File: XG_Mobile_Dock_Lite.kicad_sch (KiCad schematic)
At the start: 21 parts, among them J1 5-1775443-8, J13 39300240, J14 469911008, J17 8730, J2 20455-040E-76, J3 20455-040E-76, J4 3-2362375-4, J5 USB_C_Receptacle, SW1 SW_Push, U1 AMS1117-3.3

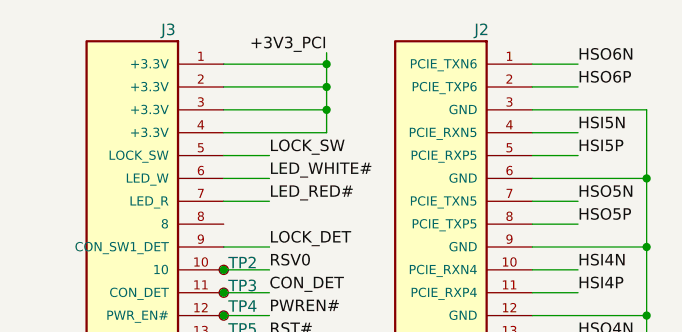
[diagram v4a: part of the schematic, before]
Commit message: pcb: fix +3.3V rail for cable LED
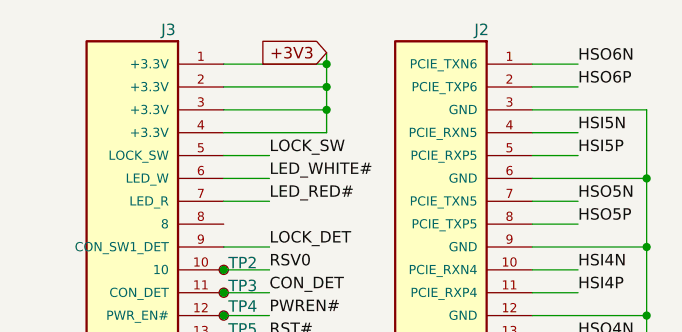
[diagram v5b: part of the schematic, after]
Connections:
- net +3V3: now also J3.1 (+3.3V), J3.2 (+3.3V), J3.3 (+3.3V), J3.4 (+3.3V)
- net +3V3_PCI: no longer J3.1 (+3.3V), J3.2 (+3.3V), J3.3 (+3.3V), J3.4 (+3.3V)
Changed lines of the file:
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@@
-		)
-	)
-	(label "+3V3_PCI"
-		(at 46.99 17.78 180)
-		(effects
-			(font
-				(size 1.27 1.27)
-			)
-			(justify right bottom)
 		)
 	)
@@
 			(effects
 				(font
+					(size 1.27 1.27)
+				)
+				(justify right)
+				(hide yes)
+			)
+		)
+	)
+	(global_label "+3V3"
+		(shape input)
+		(at 46.99 17.78 180)
+		(fields_autoplaced yes)
+		(effects
+			(font
+				(size 1.27 1.27)
+			)
+			(justify right)
+		)
+		(property "Intersheetrefs" "${INTERSHEET_REFS}"
+			(at 38.9248 17.78 0)
+			(effects
+				(font
